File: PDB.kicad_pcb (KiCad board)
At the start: 2 copper layers, 68.6 x 68.6 mm, 41 parts, among them J101 Conn_01x02_Female, J102 Conn_01x08_Female, J104 Conn_01x06_Female, U101 AZ1084-3.3, U102 MCP2562-H-SN, U103 AZ1117-5.0, U104 INA180, U105 STM32F103C8T6, Y101 8MHz

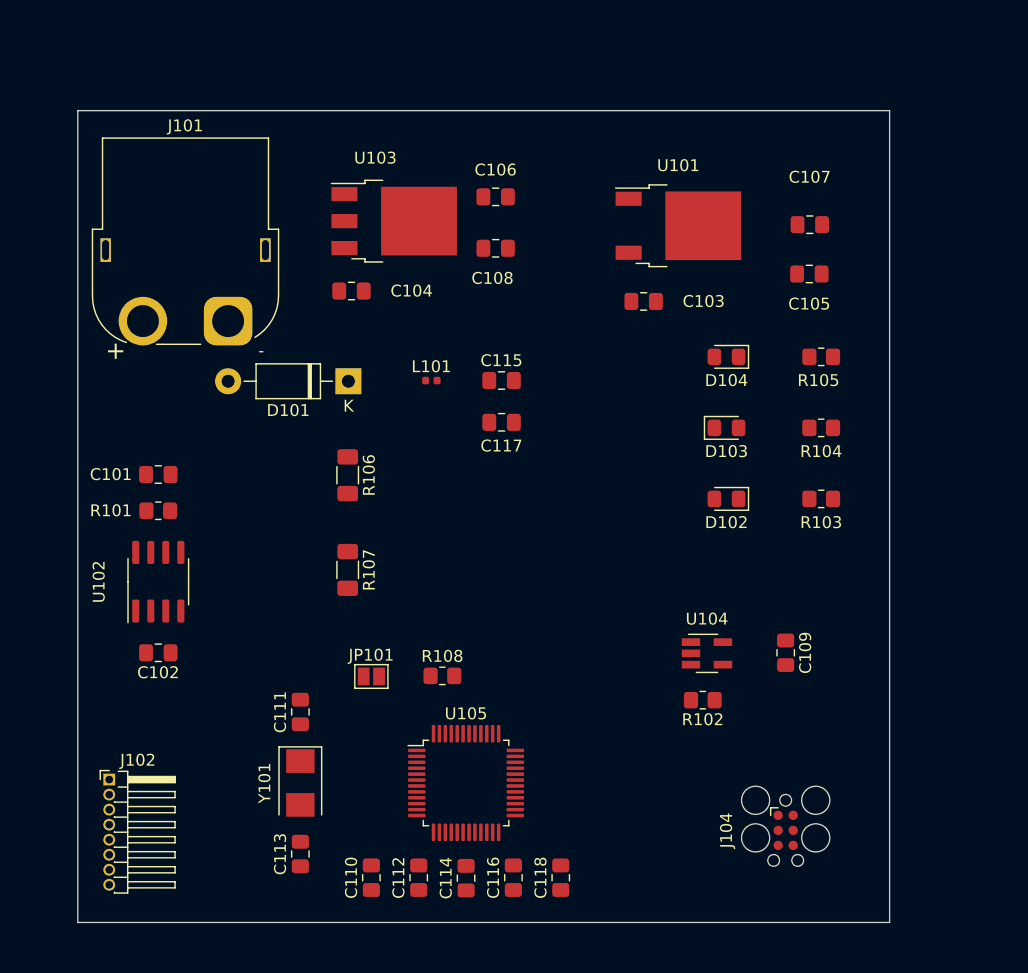
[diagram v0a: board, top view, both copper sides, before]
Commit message: rev A PCB route and silkscreen
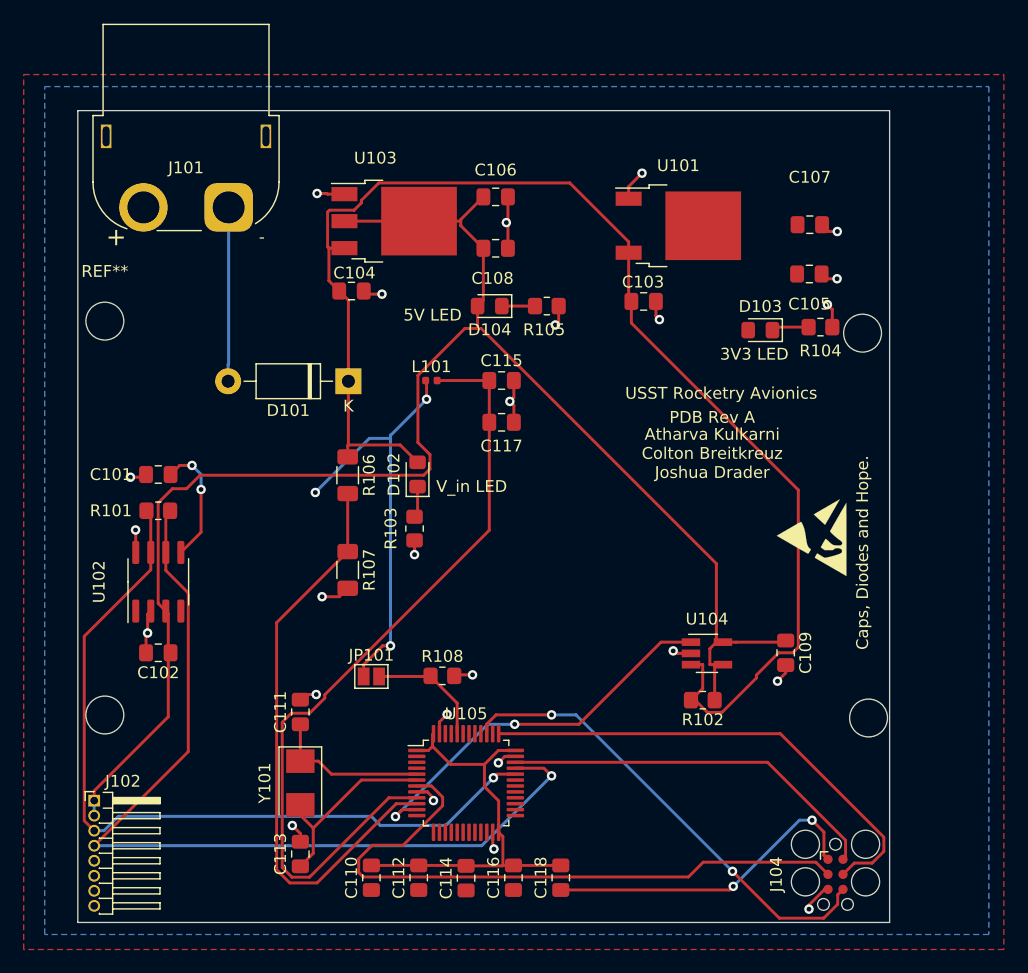
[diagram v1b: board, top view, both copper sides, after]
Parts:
- added ?: , , F.Cu at (142.5, 95.0)
- added ?: , , F.Cu at (143.0, 127.5)
- added ?: , , F.Cu at (78.5, 127.3)
- added REF**: ESD-Logo_6.6x6mm_SilkScreen, Symbol:ESD-Logo_6.6x6mm_SilkScreen, F.Cu at (138.2, 112.3)
- added REF**: MountingHole_3.2mm_M3, MountingHole:MountingHole_3.2mm_M3, F.Cu at (78.5, 94.0)
- moved R103 34.4 mm to (104.6, 111.5), turned to -90 degrees
- moved D102 26.2 mm to (104.9, 106.9), turned to 90 degrees
- moved R105 23.6 mm to (115.8, 92.7)
- moved D104 20.5 mm to (111.0, 92.7)
- moved J101 9.61 mm to (88.9, 84.4)
- moved D103 8.74 mm to (133.9, 94.7), turned to 180 degrees
- moved R104 8.51 mm to (138.9, 94.5)
- moved J104 5.61 mm to (140.2, 140.7)
- moved J102 2.18 mm to (77.6, 134.5)
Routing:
- net +5V: track 0.00 -> 138.6 mm
- net /V_in: track 0.00 -> 114.2 mm
- net /CANL: track 0.00 -> 76.9 mm, vias 0 -> 1
- net +3.3V: track 0.00 -> 73.9 mm, vias 0 -> 7
- net +3.3VA: track 0.00 -> 68.2 mm
- net /CANH: track 0.00 -> 68.0 mm, vias 0 -> 1
- net /nRESET: track 0.00 -> 54.2 mm
- net GND: track 0.00 -> 51.3 mm, vias 0 -> 25
- net /Batt_volt_sense: track 0.00 -> 49.3 mm
- net /SWCLK: track 0.00 -> 41.6 mm
- net /SWO: track 0.00 -> 39.8 mm, vias 0 -> 2
- net Net-(C110-Pad2): track 0.00 -> 35.9 mm
- net /Batt_curr_sense: track 0.00 -> 33.1 mm, vias 0 -> 2
- net /SWDIO: track 0.00 -> 32.3 mm
- net /HSE_IN: track 0.00 -> 16.5 mm
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- added copper zone on F.Cu, net +3.3V
- added copper zone on B.Cu, net GND
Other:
- board text added: "3V3 LED"
- board text added: "5V LED"
- board text added: "Atharva Kulkarni Colton Breitkreuz Joshua Drader"
- board text added: "Caps, Diodes and Hope."
- board text added: "PDB Rev A"
- board text added: "USST Rocketry Avionics"
- board text added: "V_in LED"

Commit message: more silkscreen fun
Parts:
- renumbered REF** to M3
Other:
- board text added: "3S LiPo"
- board text added: "3V3 reg"
- board text added: "5V reg"
- board text added: "<- Board I/O"
- board text added: "CAN Transciever"
- board text added: "STM header"
- board text added: "uC"
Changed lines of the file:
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@@
     (tags "mounting hole 3.2mm no annular m3")
     (attr exclude_from_pos_files exclude_from_bom)
-    (fp_text reference "REF**" (at 0 -4.2) (layer "F.SilkS")
+    (fp_text reference "M3" (at 1.016 4.318) (layer "F.SilkS")
       (effects (font (size 1 1) (thickness 0.15)))
     )
@@
     (effects (font (size 1 1) (thickness 0.15)))
   )
+  (gr_text "<- Board I/O" (at 91.186 143.256) (layer "F.SilkS")
+    (effects (font (size 1.3 1.3) (thickness 0.3)))
+  )
+  (gr_text "3V3 reg" (at 128.778 78.486) (layer "F.SilkS")
+    (effects (font (size 1.5 1.5) (thickness 0.3)))
+  )
+  (gr_text "3S LiPo" (at 84.328 88.646) (layer "F.SilkS")
+    (effects (font (size 1.5 1.5) (thickness 0.3)))
+  )
   (gr_text "USST Rocketry Avionics" (at 130.556 100.076) (layer "F.SilkS")
     (effects (font (size 1 1) (thickness 0.15)))
@@
     (effects (font (size 1 1) (thickness 0.15)))
   )
+  (gr_text "uC" (at 112.522 125.73) (layer "F.SilkS")
+    (effects (font (size 1.5 1.5) (thickness 0.3)))
+  )
+  (gr_text "CAN Transciever" (at 87.63 114.808 90) (layer "F.SilkS")
+    (effects (font (size 1.5 1.5) (thickness 0.3)))
+  )
   (gr_text "5V LED\n" (at 106.172 93.472) (layer "F.SilkS")
     (effects (font (size 1 1) (thickness 0.15)))
@@
     (effects (font (size 1 1) (thickness 0.15)))
   )
+  (gr_text "5V reg" (at 104.902 78.232) (layer "F.SilkS")
+    (effects (font (size 1.5 1.5) (thickness 0.3)))
+  )
   (gr_text "V_in LED" (at 109.474 107.95) (layer "F.SilkS")
     (effects (font (size 1 1) (thickness 0.15)))
@@
     (effects (font (size 1 1) (thickness 0.15)))
   )
+  (gr_text "STM header" (at 135.89 134.366) (layer "F.SilkS")
+    (effects (font (size 1.5 1.5) (thickness 0.3)))
+  )
   (segment (start 105.664 100.584) (end 105.664 99.079) (width 0.25) (layer "F.Cu") (net 1))
